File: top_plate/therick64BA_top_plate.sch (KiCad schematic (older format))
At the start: 74 parts, among them U1 HOLE, U10 HOLE, U11 HOLE, U12 HOLE, U13 HOLE, U14 HOLE, U15 HOLE, U16 HOLE, U17 HOLE, U18 HOLE, U19 HOLE, U2 HOLE, U20 HOLE, U21 HOLE, U22 HOLE, U23 HOLE, U24 HOLE, U25 HOLE, U26 HOLE, U27 HOLE, U28 HOLE, U29 HOLE, U3 HOLE, U30 HOLE, U31 HOLE, U32 HOLE, U33 HOLE, U34 HOLE, U35 HOLE, U36 HOLE, U37 HOLE, U38 HOLE, U39 HOLE, U4 HOLE, U40 HOLE, U41 HOLE, U42 HOLE, U43 HOLE, U44 HOLE, U45 HOLE, U46 HOLE, U47 HOLE, U48 HOLE, U49 HOLE, U5 HOLE, U50 HOLE, U51 HOLE, U52 HOLE, U53 HOLE, U54 HOLE, U55 HOLE, U56 HOLE, U57 HOLE, U58 HOLE, U59 HOLE, U6 HOLE, U60 HOLE, U61 HOLE, U62 HOLE, U63 HOLE, U64 HOLE, U7 HOLE, U8 HOLE, U9 HOLE

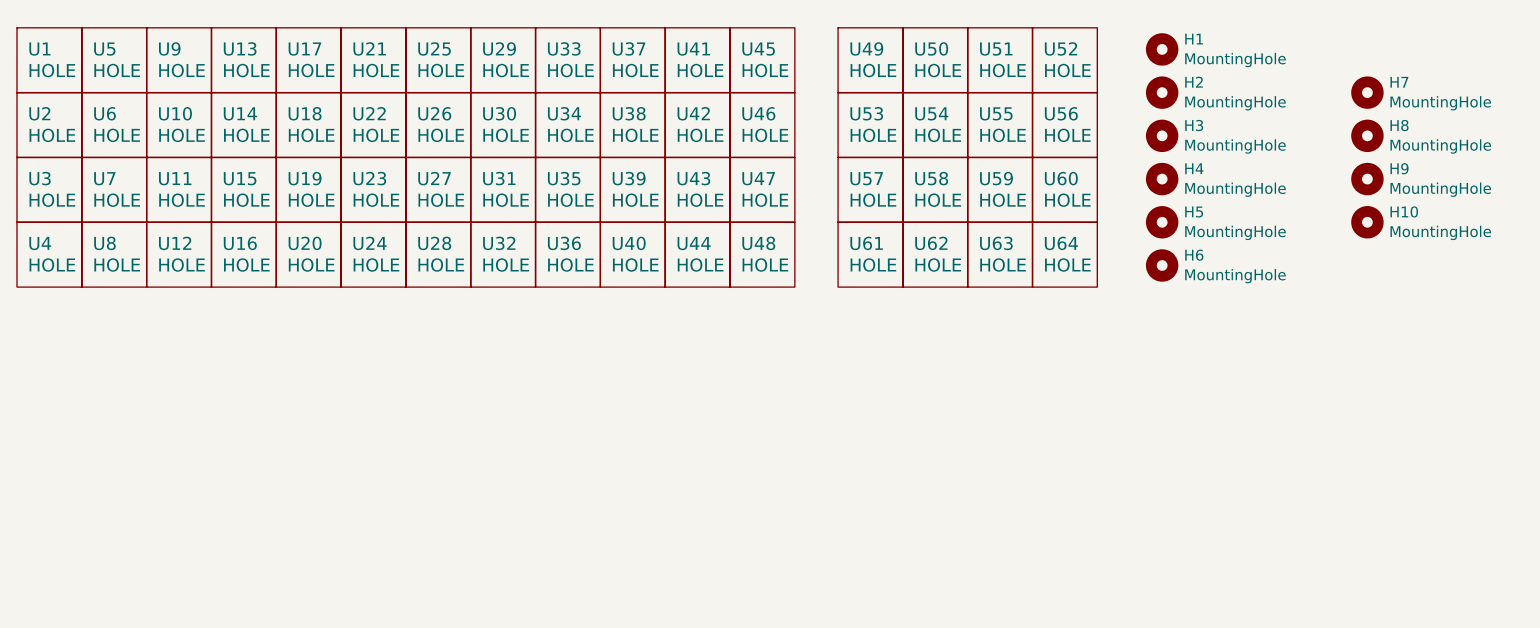
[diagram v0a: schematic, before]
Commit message: Update to 19mm
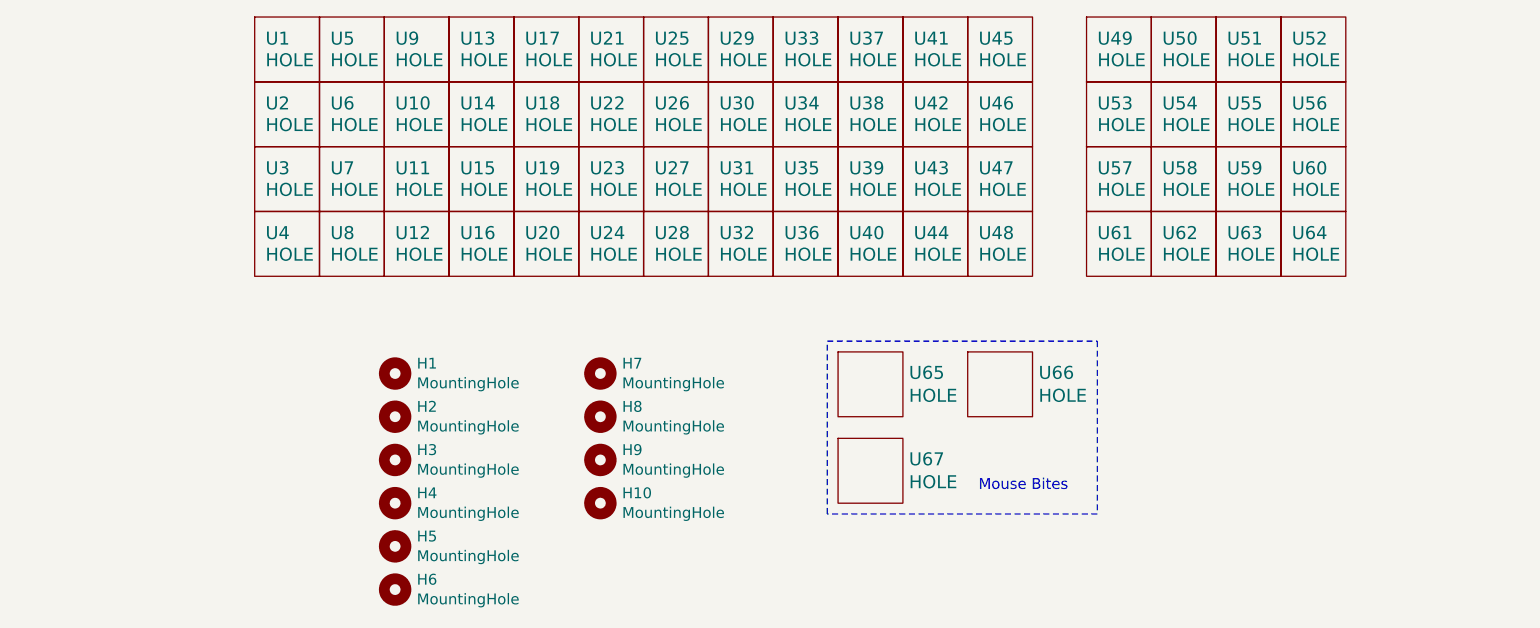
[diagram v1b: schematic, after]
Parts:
- added U65, U66, U67: HOLE, acheron_Hardware:MouseBite_IPC7351, symbol lets_split-cache:HOLE
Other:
- note added: "Mouse Bites"
- moved on the sheet: H1, H2, H3, H4, H5, H6, U1, U10, U11, U12, U13, U14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
